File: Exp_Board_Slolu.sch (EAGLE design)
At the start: 12 parts, among them Q1 Transistor 1, Q2 Transistor 2

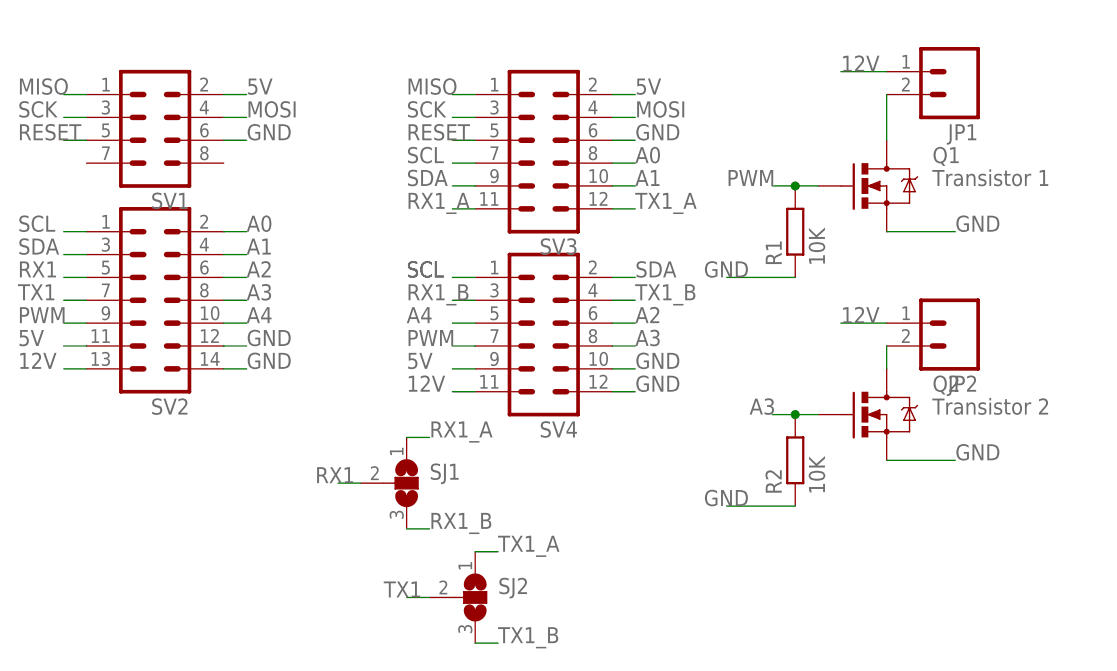
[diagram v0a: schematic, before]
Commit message: Update Exp_Board_Slolu.sch
include transistor Q1 and Q2 value
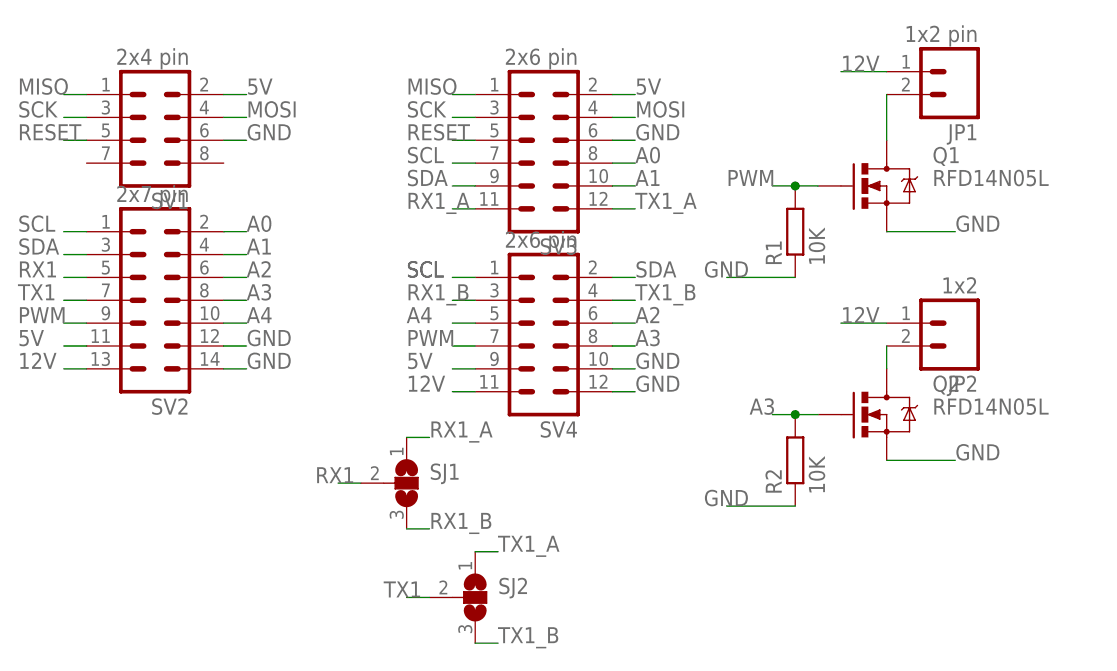
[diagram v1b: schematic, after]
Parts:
- JP1: value (none) -> 1x2 pin
- JP2: value (none) -> 1x2
- Q1: value Transistor 1 -> RFD14N05L
- Q2: value Transistor 2 -> RFD14N05L
- SV1: value (none) -> 2x4 pin
- SV2: value (none) -> 2x7 pin
- SV3, SV4: value (none) -> 2x6 pin
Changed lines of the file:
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@@
 <?xml version="1.0" encoding="utf-8"?>
 <!DOCTYPE eagle SYSTEM "eagle.dtd">
-<eagle version="6.2">
+<eagle version="6.4">
 <drawing>
 <settings>
@@
 <grid distance="0.1" unitdist="inch" unit="inch" style="lines" multiple="1" display="no" altdistance="0.01" altunitdist="inch" altunit="inch"/>
 <layers>
-<layer number="1" name="Top" color="4" fill="1" visible="yes" active="no"/>
-<layer number="2" name="Route2" color="1" fill="3" visible="yes" active="no"/>
-<layer number="3" name="Route3" color="4" fill="3" visible="yes" active="no"/>
-<layer number="4" name="Route4" color="1" fill="4" visible="yes" active="no"/>
-<layer number="5" name="Route5" color="4" fill="4" visible="yes" active="no"/>
-<layer number="6" name="Route6" color="1" fill="8" visible="yes" active="no"/>
-<layer number="7" name="Route7" color="4" fill="8" visible="yes" active="no"/>
-<layer number="8" name="Route8" color="1" fill="2" visible="yes" active="no"/>
-<layer number="9" name="Route9" color="4" fill="2" visible="yes" active="no"/>
-<layer number="10" name="Route10" color="1" fill="7" visible="yes" active="no"/>
-<layer number="11" name="Route11" color="4" fill="7" visible="yes" active="no"/>
-<layer number="12" name="Route12" color="1" fill="5" visible="yes" active="no"/>
-<layer number="13" name="Route13" color="4" fill="5" visible="yes" active="no"/>
-<layer number="14" name="Route14" color="1" fill="6" visible="yes" active="no"/>
-<layer number="15" name="Route15" color="4" fill="6" visible="yes" active="no"/>
-<layer number="16" name="Bottom" color="1" fill="1" visible="yes" active="no"/>
-<layer number="17" name="Pads" color="2" fill="1" visible="yes" active="no"/>
-<layer number="18" name="Vias" color="2" fill="1" visible="yes" active="no"/>
-<layer number="19" name="Unrouted" color="6" fill="1" visible="yes" active="no"/>
-<layer number="20" name="Dimension" color="15" fill="1" visible="yes" active="no"/>
-<layer number="21" name="tPlace" color="7" fill="1" visible="yes" active="no"/>
-<layer number="22" name="bPlace" color="7" fill="1" visible="yes" active="no"/>
-<layer number="23" name="tOrigins" color="15" fill="1" visible="yes" active="no"/>
-<layer number="24" name="bOrigins" color="15" fill="1" visible="yes" active="no"/>
-<layer number="25" name="tNames" color="7" fill="1" visible="yes" active="no"/>
-<layer number="26" name="bNames" color="7" fill="1" visible="yes" active="no"/>
-<layer number="27" name="tValues" color="7" fill="1" visible="yes" active="no"/>
-<layer number="28" name="bValues" color="7" fill="1" visible="yes" active="no"/>
+<layer number="1" name="Top" color="4" fill="1" visible="no" active="no"/>
+<layer number="2" name="Route2" color="1" fill="3" visible="no" active="no"/>
+<layer number="3" name="Route3" color="4" fill="3" visible="no" active="no"/>
+<layer number="4" name="Route4" color="1" fill="4" visible="no" active="no"/>
+<layer number="5" name="Route5" color="4" fill="4" visible="no" active="no"/>
+<layer number="6" name="Route6" color="1" fill="8" visible="no" active="no"/>
+<layer number="7" name="Route7" color="4" fill="8" visible="no" active="no"/>
+<layer number="8" name="Route8" color="1" fill="2" visible="no" active="no"/>
+<layer number="9" name="Route9" color="4" fill="2" visible="no" active="no"/>
+<layer number="10" name="Route10" color="1" fill="7" visible="no" active="no"/>
+<layer number="11" name="Route11" color="4" fill="7" visible="no" active="no"/>
+<layer number="12" name="Route12" color="1" fill="5" visible="no" active="no"/>
+<layer number="13" name="Route13" color="4" fill="5" visible="no" active="no"/>
+<layer number="14" name="Route14" color="1" fill="6" visible="no" active="no"/>
+<layer number="15" name="Route15" color="4" fill="6" visible="no" active="no"/>
+<layer number="16" name="Bottom" color="1" fill="1" visible="no" active="no"/>
+<layer number="17" name="Pads" color="2" fill="1" visible="no" active="no"/>
+<layer number="18" name="Vias" color="2" fill="1" visible="no" active="no"/>
+<layer number="19" name="Unrouted" color="6" fill="1" visible="no" active="no"/>
+<layer number="20" name="Dimension" color="15" fill="1" visible="no" active="no"/>
+<layer number="21" name="tPlace" color="7" fill="1" visible="no" active="no"/>
+<layer number="22" name="bPlace" color="7" fill="1" visible="no" active="no"/>
+<layer number="23" name="tOrigins" color="15" fill="1" visible="no" active="no"/>
+<layer number="24" name="bOrigins" color="15" fill="1" visible="no" active="no"/>
+<layer number="25" name="tNames" color="7" fill="1" visible="no" active="no"/>
+<layer number="26" name="bNames" color="7" fill="1" visible="no" active="no"/>
+<layer number="27" name="tValues" color="7" fill="1" visible="no" active="no"/>
+<layer number="28" name="bValues" color="7" fill="1" visible="no" active="no"/>
 <layer number="29" name="tStop" color="7" fill="3" visible="no" active="no"/>
 <layer number="30" name="bStop" color="7" fill="6" visible="no" active="no"/>
@@
 <layer number="35" name="tGlue" color="7" fill="4" visible="no" active="no"/>
 <layer number="36" name="bGlue" color="7" fill="5" visible="no" active="no"/>
-<layer number="37" name="tTest" color="7" fill="1" visible="yes" active="no"/>
-<layer number="38" name="bTest" color="7" fill="1" visible="yes" active="no"/>
+<layer number="37" name="tTest" color="7" fill="1" visible="no" active="no"/>
+<layer number="38" name="bTest" color="7" fill="1" visible="no" active="no"/>
 <layer number="39" name="tKeepout" color="4" fill="11" visible="no" active="no"/>
 <layer number="40" name="bKeepout" color="1" fill="11" visible="no" active="no"/>
@@
 <layer number="44" name="Drills" color="7" fill="1" visible="no" active="no"/>
 <layer number="45" name="Holes" color="7" fill="1" visible="no" active="no"/>
-<layer number="46" name="Milling" color="3" fill="1" visible="yes" active="no"/>
-<layer number="47" name="Measures" color="7" fill="1" visible="yes" active="no"/>
-<layer number="48" name="Document" color="7" fill="1" visible="yes" active="no"/>
-<layer number="49" name="Reference" color="7" fill="1" visible="yes" active="no"/>
-<layer number="50" name="dxf" color="7" fill="1" visible="yes" active="no"/>
-<layer number="51" name="tDocu" color="7" fill="1" visible="yes" active="no"/>
-<layer number="52" name="bDocu" color="7" fill="1" visible="yes" active="no"/>
-<layer number="53" name="tGND_GNDA" color="7" fill="9" visible="yes" active="no"/>
-<layer number="54" name="bGND_GNDA" color="1" fill="9" visible="yes" active="no"/>
-<layer number="56" name="wert" color="7" fill="1" visible="yes" active="no"/>
+<layer number="46" name="Milling" color="3" fill="1" visible="no" active="no"/>
+<layer number="47" name="Measures" color="7" fill="1" visible="no" active="no"/>
+<layer number="48" name="Document" color="7" fill="1" visible="no" active="no"/>
+<layer number="49" name="Reference" color="7" fill="1" visible="no" active="no"/>
+<layer number="50" name="dxf" color="7" fill="1" visible="no" active="no"/>
+<layer number="51" name="tDocu" color="7" fill="1" visible="no" active="no"/>
+<layer number="52" name="bDocu" color="7" fill="1" visible="no" active="no"/>
+<layer number="53" name="tGND_GNDA" color="7" fill="9" visible="no" active="no"/>
+<layer number="54" name="bGND_GNDA" color="1" fill="9" visible="no" active="no"/>
+<layer number="56" name="wert" color="7" fill="1" visible="no" active="no"/>
 <layer number="91" name="Nets" color="2" fill="1" visible="yes" active="yes"/>
 <layer number="92" name="Busses" color="1" fill="1" visible="yes" active="yes"/>
@@
 </classes>
 <parts>
-<part name="SV1" library="con-lstb" deviceset="MA04-2" device=""/>
-<part name="SV2" library="con-lstb" deviceset="MA07-2" device=""/>
-<part name="SV3" library="con-lstb" deviceset="MA06-2" device=""/>
-<part name="Q1" library="SparkFun-DiscreteSemi" deviceset="MOSFET-NCHANNEL" device="PTH2" value="Transistor 1"/>
-<part name="Q2" library="SparkFun-DiscreteSemi" deviceset="MOSFET-NCHANNEL" device="PTH2" value="Transistor 2"/>
+<part name="SV1" library="con-lstb" deviceset="MA04-2" device="" value="2x4 pin"/>
+<part name="SV2" library="con-lstb" deviceset="MA07-2" device="" value="2x7 pin"/>
+<part name="SV3" library="con-lstb" deviceset="MA06-2" device="" value="2x6 pin"/>
+<part name="Q1" library="SparkFun-DiscreteSemi" deviceset="MOSFET-NCHANNEL" device="PTH2" value="RFD14N05L"/>
+<part name="Q2" library="SparkFun-DiscreteSemi" deviceset="MOSFET-NCHANNEL" device="PTH2" value="RFD14N05L"/>
 <part name="R2" library="resistor" deviceset="R-EU_" device="0204/7" value="10K"/>
 <part name="R1" library="resistor" deviceset="R-EU_" device="0204/7" value="10K"/>
-<part name="JP1" library="SparkFun-Connectors" deviceset="M02" device="PTH"/>
-<part name="JP2" library="SparkFun-Connectors" deviceset="M02" device="PTH"/>
-<part name="SV4" library="con-lstb" deviceset="MA06-2" device=""/>
+<part name="JP1" library="SparkFun-Connectors" deviceset="M02" device="PTH" value="1x2 pin"/>
+<part name="JP2" library="SparkFun-Connectors" deviceset="M02" device="PTH" value="1x2"/>
+<part name="SV4" library="con-lstb" deviceset="MA06-2" device="" value="2x6 pin"/>
 <part name="SJ1" library="jumper" deviceset="SJ2W" device=""/>
 <part name="SJ2" library="jumper" deviceset="SJ2W" device=""/>
